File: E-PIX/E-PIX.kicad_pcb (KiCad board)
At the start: 6 copper layers, 40 x 40 mm, 47 parts, among them J1 USB_C_Receptacle_USB2.0, J2 BNO055, J3 ADC, J4 ADC, Q1 BSS138, Q2 BSS138, SW1 SW, SW2 SW_Push, U1 Conn_03x04, U2 Conn_03x04, U3 TC7WH241FK, U4 TC7WH241FK, U5 NJM7805SDL1, U6 AZ1117-3.3, U7 ESP32-C3-WROOM-02, U8 BTS6142D

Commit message: finish eeschema. start placing tips
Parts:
- removed G***: LOGO, Logo:Robo
- removed G***: LOGO, Logo:L6
- removed J3, J4: ADC, Connector_PinHeader_2.54mm:PinHeader_1x03_P2.54mm_Vertical
- added C10: 10u/50V/2012, Capacitor_SMD:C_0805_2012Metric, F.Cu at (123.2, 107.6)
- added C11: 22u/25V/2012, Capacitor_SMD:C_0805_2012Metric, F.Cu at (123.2, 89.8)
- added C12: 0.1u/25V, Capacitor_SMD:C_0603_1608Metric, B.Cu at (157.9, 101.3)
- added C9: 0.1u/25V, Capacitor_SMD:C_0603_1608Metric, B.Cu at (152.6, 89.8)
- added D4: CUHS20S60/2A/60V, Diode:Diode_US2H, F.Cu at (124.8, 115.9)
- added D5: CUHS20S60/2A/60V, Diode:Diode_US2H, F.Cu at (123.5, 94.9)
- added D6: CUHS20S60/2A/60V, Diode:Diode_US2H, F.Cu at (123.5, 98.7)
- added D7: LED, LED_SMD:LED_0603_1608Metric, B.Cu at (142.9, 91.0)
- added D8: WS2812B, LED_SMD:LED_WS2812B_PLCC4_5.0x5.0mm_P3.2mm, B.Cu at (145.4, 84.0)
- added Q3: AO3401A, Package_TO_SOT_SMD:SOT-23, F.Cu at (130.8, 93.7)
- added Q4: BSS138, Package_TO_SOT_SMD:SOT-23, F.Cu at (147.8, 129.8)
- added Q5: BSS138, Package_TO_SOT_SMD:SOT-23, F.Cu at (152.9, 129.8)
- added R14: 4.7, Resistor_SMD:R_0603_1608Metric, F.Cu at (128.4, 97.5)
- added R15: 2.2k, Resistor_SMD:R_0603_1608Metric, F.Cu at (149.2, 134.9)
- added R16: 2.2k, Resistor_SMD:R_0603_1608Metric, F.Cu at (141.7, 127.3)
- added R17: 2.2k, Resistor_SMD:R_0603_1608Metric, F.Cu at (137.3, 130.5)
- added R18: 2.2k, Resistor_SMD:R_0603_1608Metric, F.Cu at (141.7, 129.8)
- added R19: 10k, Resistor_SMD:R_0603_1608Metric, B.Cu at (157.6, 102.5)
- added R20: 100, Resistor_SMD:R_0603_1608Metric, B.Cu at (141.5, 94.9)
- added U10: Conn_03x04, Conn:PinHeader_03x04_P2.54mm_Vertical, F.Cu at (153.3, 122.9)
- C1: value 1u/50V/2012 -> 10u/35V; footprint Capacitor_SMD:C_0805_2012Metric -> Capacitor_SMD:C_1206_3216Metric
- C2: value 10u/50V/2012 -> C_Polarized; footprint Capacitor_SMD:C_0805_2012Metric -> Capacitor_THT:CP_Radial_D8.0mm_P3.50mm
- C3: value 10u/35V -> 47p; footprint Capacitor_SMD:C_0603_1608Metric -> Capacitor_SMD:C_0201_0603Metric
- C4: value 0.1u/25V -> 47p; footprint Capacitor_SMD:C_0603_1608Metric -> Capacitor_SMD:C_0201_0603Metric
- C5: value 22u/25V/2012 -> 0.1u/25V; footprint Capacitor_SMD:C_0805_2012Metric -> Capacitor_SMD:C_0603_1608Metric
- C6: value 1u/16V -> 1u/50V/2012; footprint Capacitor_SMD:C_0603_1608Metric -> Capacitor_SMD:C_0805_2012Metric
- C8, R9: moved to B.Cu
- D2: value CUHS20S60/2A/60V -> LED; footprint Diode:Diode_US2H -> LED_SMD:LED_0603_1608Metric; moved to B.Cu
- D3: value GREEN -> LED; moved to B.Cu
- J1: footprint Connector_USB:USB_C_Receptacle_XKB_U262-16XN-4BVC11 -> Connector_USB:USB_C_Receptacle_XKB_U262-16XN-4BVC11_with_model
- J2: value BNO055 -> DM3AT-SF-PEJM5; footprint Connector_PinHeader_2.54mm:PinHeader_1x05_P2.54mm_Vertical -> Connector_Card:microSD_HC_Hirose_DM3AT-SF-PEJM5
- Q1, Q2: value BSS138 -> 2SC4213; footprint Package_TO_SOT_SMD:SOT-23 -> Package_TO_SOT_SMD:SOT-323_SC-70
- R1: value 10k -> 5.1k
- R10: value 10k -> 47k
- R11: value 510 -> 47k
- R12, R13: value 2.2k -> 470k
- R3: value 5.1k -> 27
- R4: value 10k -> 27
- R5: value 2.2k -> 10k
- R6: value 2.2k -> 100; moved to B.Cu
- R8: value 10k -> 100; moved to B.Cu
- SW1: value SW -> SW_Push; footprint Connector_PinHeader_2.54mm:PinHeader_1x02_P2.54mm_Vertical -> Button_Switch_SMD:SKRPACE010; moved to B.Cu
- SW2: footprint Button_Switch_SMD:SW_Push_1P1T_NO_Vertical_Wuerth_434133025816 -> Button_Switch_SMD:SKRPACE010; moved to B.Cu
- U1: value Conn_03x04 -> FT231XS; footprint Conn:PinHeader_03x04_P2.54mm_Vertical -> Package_SO:SSOP-20_3.9x8.7mm_P0.635mm
- U2: value Conn_03x04 -> ESP32-S3-WROOM-1; footprint Conn:PinHeader_03x04_P2.54mm_Vertical -> Espressif:ESP32-S3-WROOM-1
- U3: value TC7WH241FK -> BTS6142D; footprint Logic:US-8 -> Package_TO_SOT_SMD:TO-252-4
- U4: value TC7WH241FK -> NJM7805SDL1; footprint Logic:US-8 -> Package_TO_SOT_SMD:TO-252-2
- U5: value NJM7805SDL1 -> TC7WH241FK; footprint Package_TO_SOT_SMD:TO-252-2 -> Logic:US-8
- U6: value AZ1117-3.3 -> TC7WH241FK; footprint Package_TO_SOT_SMD:SOT-223-3_TabPin2 -> Logic:US-8
- U7: value ESP32-C3-WROOM-02 -> AZ1117-3.3; footprint Espressif:ESP32-C3-WROOM-02 -> Package_TO_SOT_SMD:SOT-223-3_TabPin2
- U8: value BTS6142D -> ~; footprint Package_TO_SOT_SMD:TO-252-4 -> IMU:BNO055; moved to B.Cu
- U9: value ~ -> Conn_03x02; footprint IMU:BNO055 -> Conn:PinHeader_03x02_P2.54mm_Vertical; moved to F.Cu
- moved SW2 68.7 mm to (162.1, 102.5), turned to 90 degrees
- moved R5 67.2 mm to (156.7, 117.8), turned to 0 degrees
- moved H1 64.6 mm to (162.4, 122.4)
- moved H4 64.6 mm to (128.4, 122.4)
- moved R7 58.4 mm to (157.6, 120.3)
- moved U3 57.2 mm to (153.6, 109.7), turned to 90 degrees
- moved C2 54.5 mm to (161.0, 114.0), turned to -90 degrees
- moved J2 54.4 mm to (134.2, 109.9), turned to -90 degrees
- moved U4 54.0 mm to (136.0, 121.3), turned to 180 degrees
- moved C8 53.8 mm to (152.6, 92.4)
- moved R4 53.2 mm to (170.3, 97.5), turned to 0 degrees
- moved R11 52.7 mm to (147.4, 105.1), turned to 0 degrees
- moved U9 50.3 mm to (145.7, 108.9), turned to 0 degrees
- moved Q2 49.0 mm to (146.0, 103.8), turned to 0 degrees
- moved H2 48.7 mm to (162.4, 108.9)
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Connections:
- C1 pad 2: VDD -> +3V3
- C2 pad 1: GND -> VDD
- C2 pad 2: +5V -> GND
- C3 pad 1: +3V3 -> GND
- C3 pad 2: GND -> Net-(U1-USBDM)
- C4 pad 1: +5V -> GND
- C4 pad 2: GND -> Net-(U1-USBDP)
- C5 pad 1: +3V3 -> GND
- C5 pad 2: GND -> +3V3
- C6 pad 1: Net-(U7-EN/CHIP_PU) -> GND
- C6 pad 2: GND -> VSS
- C7 pad 1: +3V3 -> +5V
- C8 pad 1: /RST -> /EN
- D1 pad 1: VDD -> +5V
- D1 pad 2: +5V -> Net-(D1-A)
- D2 pad 1: +5V -> Net-(D2-K)
- D2 pad 2: Net-(D2-A) -> VSS
- D3 pad 1: GND -> Net-(D3-K)
- D3 pad 2: Net-(D3-A) -> +3V3
- J1 pad A4: Net-(D2-A) -> Net-(D1-A)
- J1 pad A9: Net-(D2-A) -> Net-(D1-A)
- J1 pad B4: Net-(D2-A) -> Net-(D1-A)
- J1 pad B9: Net-(D2-A) -> Net-(D1-A)
- J1 pad S1: unconnected-(J1-SHIELD-PadS1) -> GND
- J2 pad 1: GND -> unconnected-(J2-DAT2-Pad1)
- J2 pad 2: +3V3 -> /CS
- J2 pad 3: /SCL -> /MOSI
- J2 pad 4: /SDA -> +3V3
- J2 pad 5: /BNO055RST -> /CLK
- Q1 pad 1: +3V3 -> Net-(Q1-B)
- Q1 pad 2: /ICS1_3V3 -> /RTS
- Q1 pad 3: /ICS1_5V -> /EN
- Q2 pad 1: +3V3 -> Net-(Q2-B)
- Q2 pad 2: /ICS2_3V3 -> /DTR
- Q2 pad 3: /ICS2_5V -> /BOOT
- R1 pad 1: GND -> Net-(J1-CC1)
- R1 pad 2: /ADC1 -> GND
- R10 pad 1: Net-(U8-IS) -> Net-(Q1-B)
- R10 pad 2: GND -> /DTR
- R11 pad 1: +3V3 -> Net-(Q2-B)
- R11 pad 2: Net-(D3-A) -> /RTS
- R12 pad 1: +5V -> GND
- R12 pad 2: /ICS1_5V -> /DTR
- R13 pad 1: +5V -> GND
- R13 pad 2: /ICS2_5V -> /RTS
- R2 pad 1: Net-(J1-CC1) -> Net-(J1-CC2)
- R3 pad 1: Net-(J1-CC2) -> /D-
- R3 pad 2: GND -> Net-(U1-USBDM)
- R4 pad 1: GND -> Net-(U1-USBDP)
- R4 pad 2: /ADC2 -> /D+
- R5 pad 1: +3V3 -> Net-(U3-IN)
- R5 pad 2: /ICS1_3V3 -> /EN_Power
- R6 pad 1: +3V3 -> Net-(D2-K)
- R6 pad 2: /ICS2_3V3 -> GND
- R7 pad 1: +3V3 -> Net-(U3-IS)
- R7 pad 2: Net-(U7-EN/CHIP_PU) -> GND
- R8 pad 1: +3V3 -> Net-(D3-K)
- R8 pad 2: Net-(U7-GPIO8) -> GND
- R9 pad 1: Net-(SW1A-B) -> /EN
- R9 pad 2: Net-(U8-IN) -> +3V3
- SW1 pad 1: GND -> /EN
- SW1 pad 2: Net-(SW1A-B) -> GND
- SW2 pad 1: /RST -> /SW
- U1 pad 1: GND -> /DTR
- U1 pad 2: VSS -> /RTS
- U1 pad 3: /ICS1_5V -> +3V3
- U2 pad 2: VSS -> +3V3
- U2 pad 3: /ICS2_5V -> /EN
- U3 pad 1: /EN1 -> VSS
- U3 pad 2: /ICS1_3V3 -> Net-(U3-IN)
- U3 pad 3: /ICS1_3V3 -> VDD
- U3 pad 4: GND -> Net-(U3-IS)
- U3 pad 5: /TX1 -> VSS
- U4 pad 1: /EN2 -> VSS
- U4 pad 2: /ICS2_3V3 -> GND
- U4 pad 3: /ICS2_3V3 -> +5V
- U5 pad 1: VDD -> /EN1
- U5 pad 2: GND -> /ICS1_3V3
- U5 pad 3: +5V -> /ICS1_3V3
- U6 pad 1: GND -> /EN2
- U6 pad 2: +3V3 -> /ICS2_3V3
- U6 pad 3: +5V -> /ICS2_3V3
- U7 pad 1: +3V3 -> GND
- U7 pad 2: Net-(U7-EN/CHIP_PU) -> +3V3
- U7 pad 3: /ADC1 -> VSS
- U8 pad 1: VSS -> +3V3
- U8 pad 2: Net-(U8-IN) -> GND
- U8 pad 3: VDD -> /SDA
- U8 pad 4: Net-(U8-IS) -> /SCL
- U8 pad 5: VSS -> /BNO_RST
- U9 pad 1: +3V3 -> GND
- U9 pad 2: GND -> VSS
- U9 pad 3: /SDA -> /ICS1_5V
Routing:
- net +3V3: track 93.1 -> 0.00 mm
- net /BNO055RST: track 57.5 -> 0.00 mm, vias 2 -> 0
- net +5V: track 48.6 -> 0.00 mm, vias 3 -> 0
- net /EN2: track 39.6 -> 0.00 mm, vias 2 -> 0
- net /RST: track 33.9 -> 0.00 mm, vias 2 -> 0
- net /RX2: track 33.8 -> 0.00 mm, vias 2 -> 0
- net /RX1: track 31.4 -> 0.00 mm, vias 2 -> 0
- net /TX1: track 31.3 -> 0.00 mm, vias 2 -> 0
- net /EN1: track 29.6 -> 0.00 mm, vias 2 -> 0
- net /TX2: track 28.2 -> 0.00 mm, vias 2 -> 0
- net /SDA: track 25.9 -> 0.00 mm, vias 1 -> 0
- net VDD: track 25.7 -> 0.00 mm, vias 2 -> 0
- net /SCL: track 25.0 -> 0.00 mm, vias 1 -> 0
- net Net-(D2-A): track 21.5 -> 0.00 mm, vias 3 -> 0
- net /ICS1_5V: track 21.2 -> 0.00 mm, vias 2 -> 0
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- removed copper zone on B.Cu, net GND
- removed copper zone on F.Cu, net GND
- removed copper zone on In1.Cu, net GND
- removed copper zone on In2.Cu, net GND
- removed copper zone on In3.Cu, net GND
- removed copper zone on In4.Cu, net GND
- removed copper zone on F.Cu, net VDD
- removed copper zone on B.Cu, net VSS
- removed copper zone on F.Cu, net VSS
- removed copper zone on In1.Cu, net VSS
- removed copper zone on In2.Cu, net VSS
- removed copper zone on In3.Cu, net VSS
- removed copper zone on In4.Cu, net VSS
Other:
- board size 40 x 40 mm -> 40.1 x 45 mm
- copper layers 6 -> 2
- board text removed: "+"
- board text removed: "-"
- board text removed: "2024.04.06"
- board text removed: "ADC1/3V3/GND"
- board text removed: "ADC2/3V3/GND"
- board text removed: "AE-BNO055-BO"
- board text removed: "BRST/SDA/SCL/3V3/GND"
- board text removed: "CPU"
- board text removed: "ControlBoard3"
- board text removed: "GND/VDD/ICS2"
- board text removed: "HumanRobot"
- board text removed: "ICS1/VDD/GND"
- board text removed: "RESET"
- board text removed: "SW"
- board text removed: "VIN"

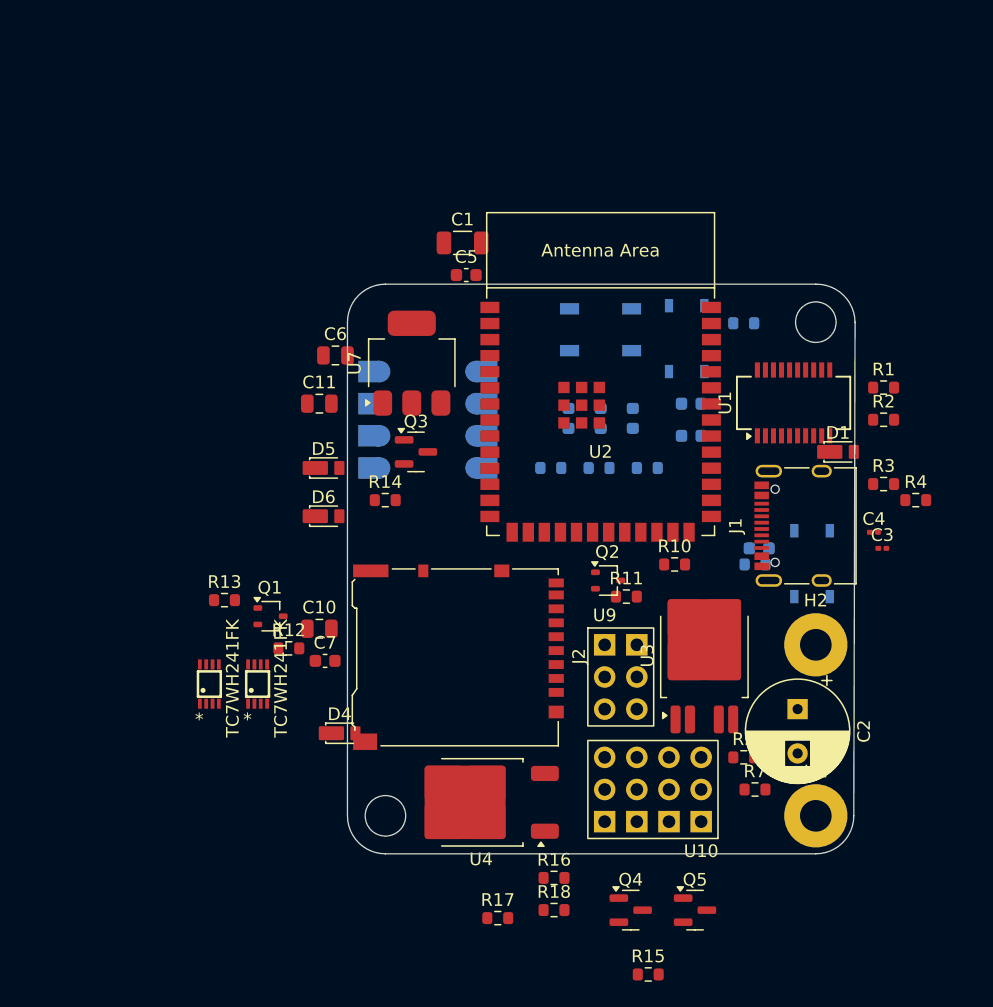
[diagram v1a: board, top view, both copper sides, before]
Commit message: place 3v3 reg and USB-TTY serial
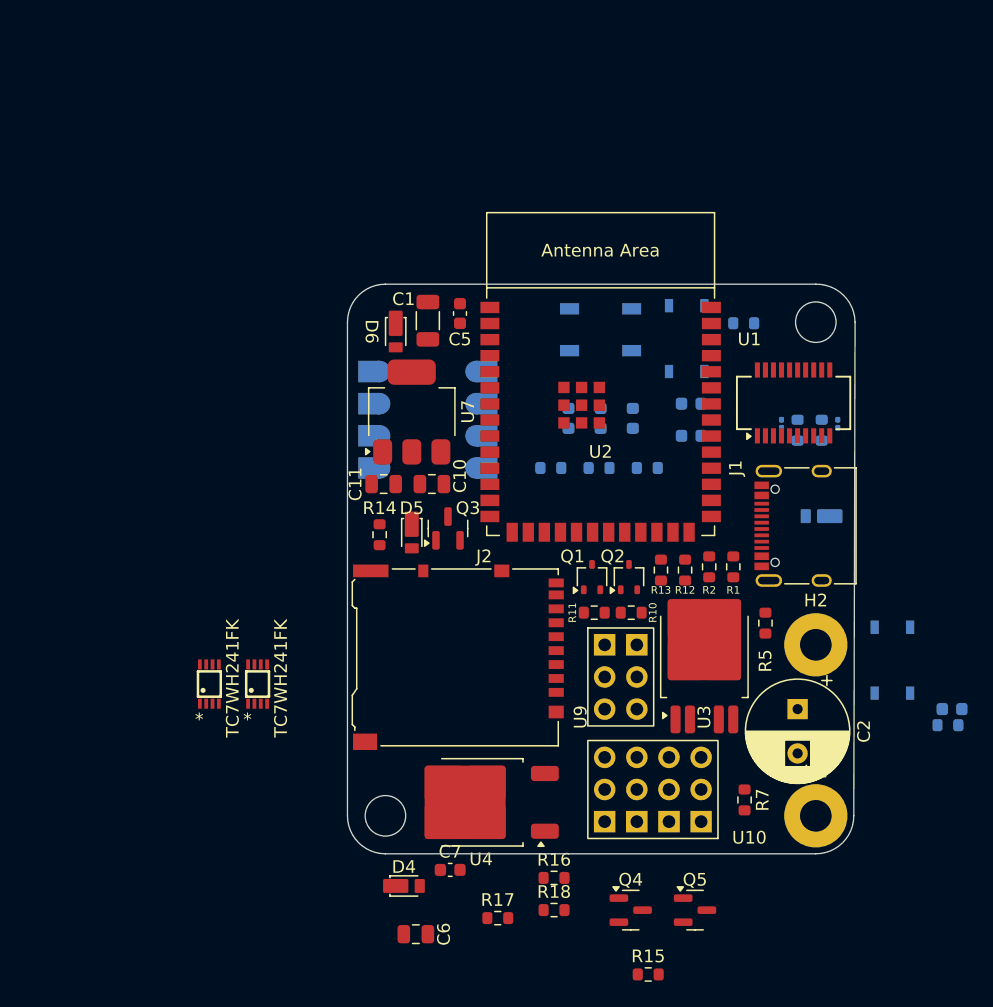
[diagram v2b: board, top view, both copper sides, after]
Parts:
- C3, C4, D1, R3, R4: moved to B.Cu
- moved C6 46.2 mm to (130.8, 131.8)
- moved R13 34.6 mm to (150.2, 103.0), turned to 90 degrees
- moved R12 31.9 mm to (152.1, 103.0), turned to 90 degrees
- moved Q1 25.6 mm to (144.7, 103.5), turned to 90 degrees
- moved R19 19.8 mm to (172.8, 115.2)
- moved C12 19.8 mm to (173.2, 114.0)
- moved C7 19.2 mm to (133.5, 126.7)
- moved R1 18.5 mm to (155.9, 102.7), turned to -90 degrees
- moved R2 18.0 mm to (154.0, 102.7), turned to -90 degrees
- moved D6 15.7 mm to (129.2, 84.1), turned to -90 degrees
- moved C10 14.5 mm to (132.1, 96.2)
- moved D4 13.1 mm to (129.9, 127.9)
- moved C3 12.7 mm to (159.7, 91.4), turned to 90 degrees
- moved R5 10.7 mm to (158.4, 107.2), turned to 90 degrees
- moved SW2 9.92 mm to (168.4, 110.1)
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
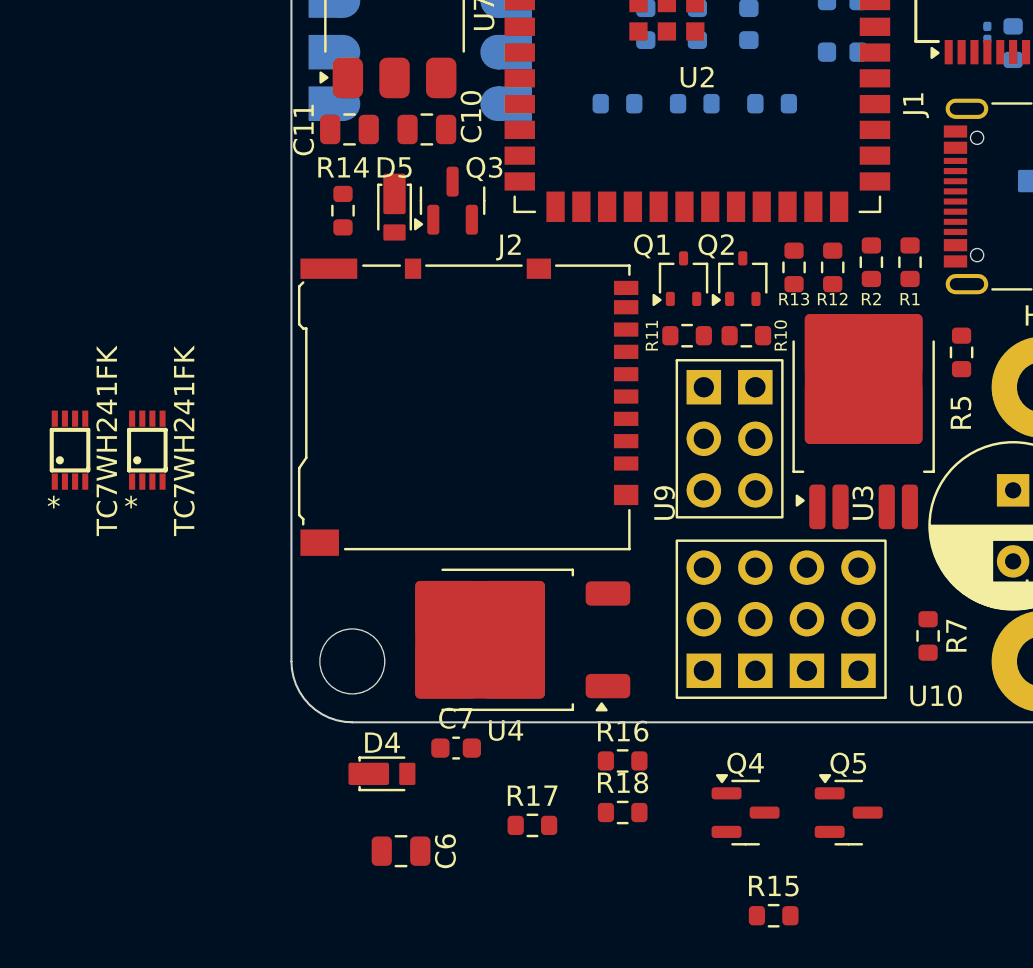
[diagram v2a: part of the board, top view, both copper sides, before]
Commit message: update some pin mappings of ESP
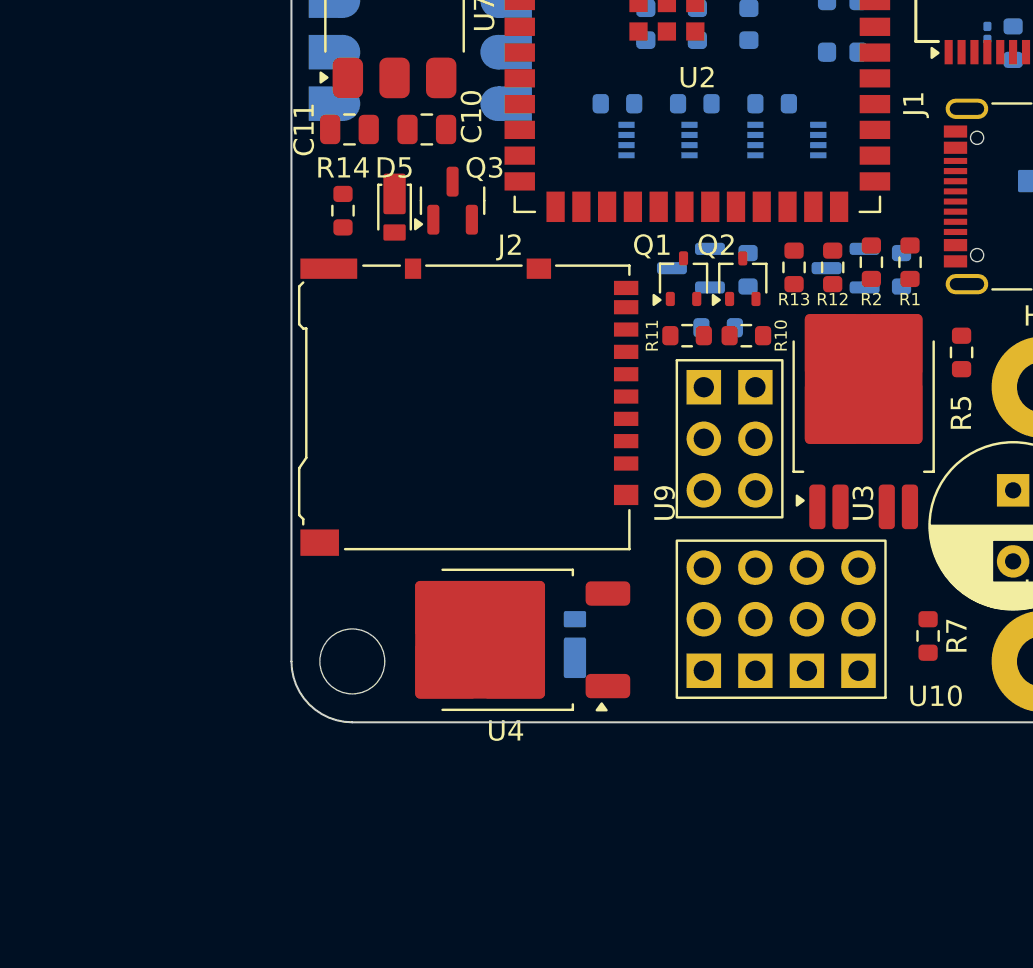
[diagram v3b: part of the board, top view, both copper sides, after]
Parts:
- C6, C7, D4, Q4, Q5, R15, R16, R17, R18, U5, U6: moved to B.Cu
- moved U6 35.0 mm to (149.8, 96.7), turned to -90 degrees
- moved R17 32.9 mm to (155.5, 103.1), turned to -90 degrees
- moved U5 32.8 mm to (143.5, 96.7), turned to -90 degrees
- moved R15 31.8 mm to (147.9, 103.1), turned to -90 degrees
- moved Q4 27.0 mm to (145.1, 103.0), turned to 180 degrees
- moved R18 26.9 mm to (154.0, 105.9), turned to 180 degrees
- moved Q5 26.8 mm to (152.7, 103.0), turned to 180 degrees
- moved R16 21.9 mm to (146.4, 106.0), turned to 180 degrees
- moved D4 11.4 mm to (139.4, 121.6), turned to 90 degrees
- moved C6 10.2 mm to (135.9, 122.9)
- moved C7 6.84 mm to (136.1, 120.3), turned to 180 degrees
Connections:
- U2 pad 22: unconnected-(U2-IO14-Pad22) -> /EN1
- U2 pad 23: unconnected-(U2-IO21-Pad23) -> /EN2
- U2 pad 26: unconnected-(U2-IO45-Pad26) -> /EN_Power
- U2 pad 28: unconnected-(U2-IO35-Pad28) -> /SW
- U2 pad 39: /SW -> unconnected-(U2-IO1-Pad39)
- U2 pad 4: /EN1 -> unconnected-(U2-IO4-Pad4)
- U2 pad 5: /EN2 -> unconnected-(U2-IO5-Pad5)
- U2 pad 6: /EN_Power -> unconnected-(U2-IO6-Pad6)

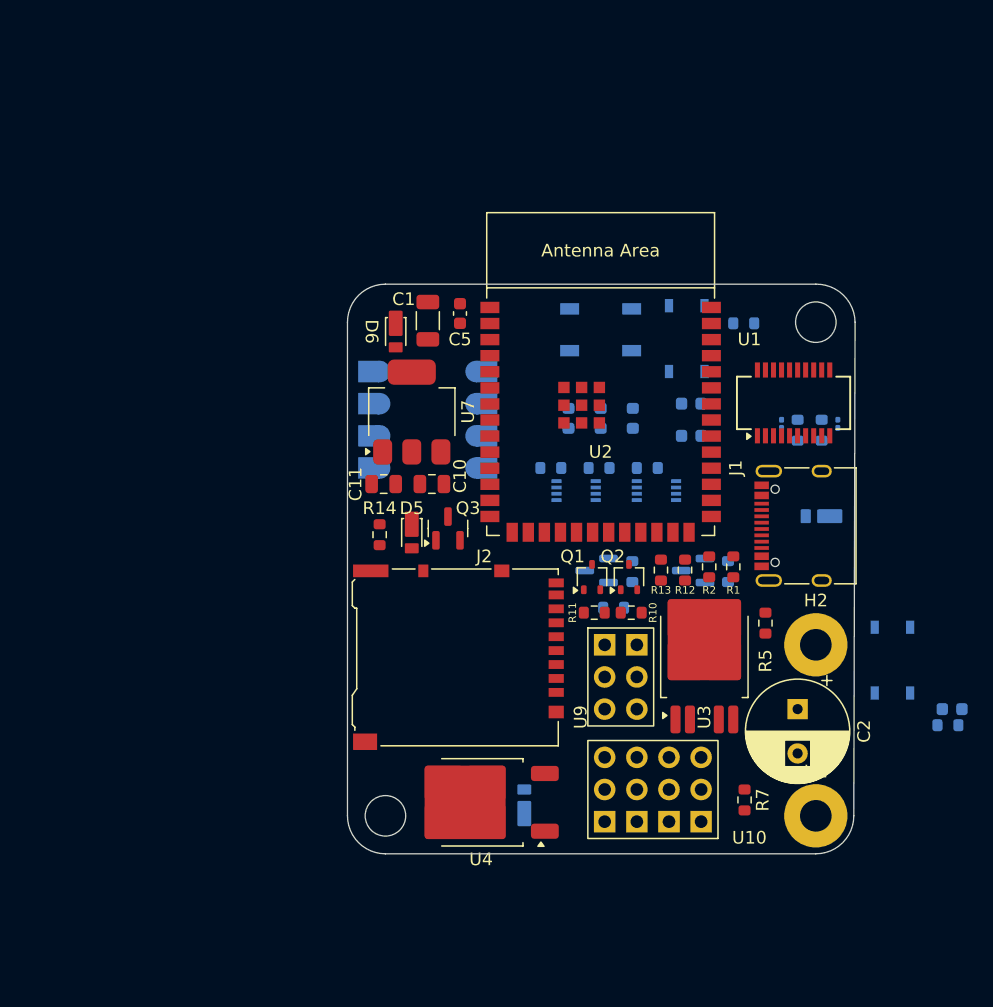
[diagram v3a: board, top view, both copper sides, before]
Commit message: place all the tips
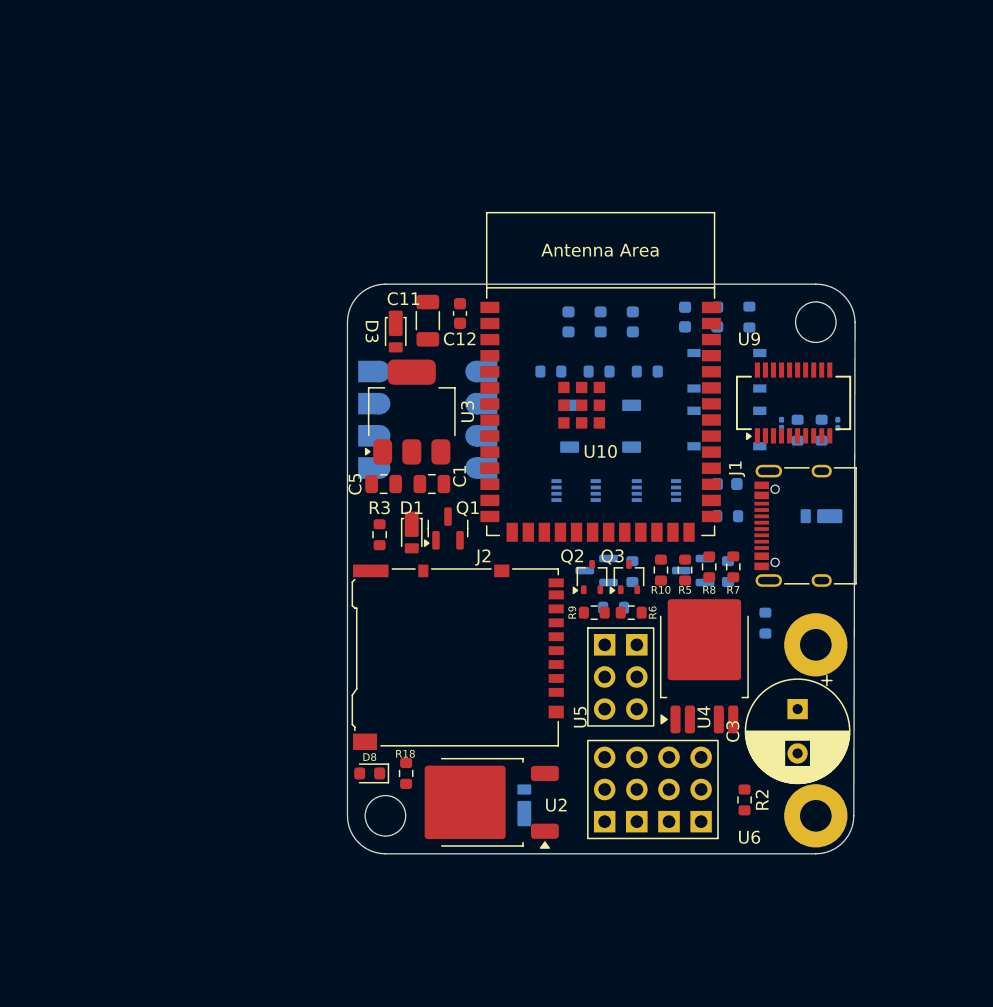
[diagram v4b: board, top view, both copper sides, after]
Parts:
- added D8: LED, LED_SMD:LED_0603_1608Metric, F.Cu at (127.2, 119.0)
- added R18: 10k, Resistor_SMD:R_0603_1608Metric, F.Cu at (130.0, 119.0)
- R1: renamed from R5; moved to B.Cu
- U7: renamed from U5; value TC7WH241FK -> U7
- U8: renamed from U6; value TC7WH241FK -> U8
- moved C6 25.1 mm to (155.4, 96.2)
- moved R11 24.0 mm to (155.4, 98.7), turned to 0 degrees
- moved SW1 22.5 mm to (155.4, 91.8), turned to 180 degrees
- moved C9 9.40 mm to (152.1, 83.0), turned to 90 degrees
- moved D4 7.62 mm to (147.9, 83.4)
- moved D6 7.62 mm to (145.4, 91.6)
- moved D7 7.62 mm to (142.9, 83.4)
- moved D9 7.62 mm to (145.4, 83.4)
- moved R14 7.62 mm to (141.5, 87.3)
- moved R19 7.62 mm to (145.3, 87.3)
- moved R4 7.62 mm to (149.1, 87.3)
- moved C10 7.14 mm to (154.6, 83.0), turned to 90 degrees
- moved SW2 4.07 mm to (155.4, 87.2), turned to 180 degrees
- moved R15 0.67 mm to (157.2, 83.0), turned to 90 degrees
- renumbered C10 to C1, C9 to C10, C1 to C11, C5 to C12, C6 to C2, C2 to C3, C7 to C4, C11 to C5, C12 to C6, C3 to C7, C4 to C8, C8 to C9, D5 to D1, D4 to D2, D6 to D3, D2 to D4, D1 to D5, D8 to D6, D3 to D9, Q3 to Q1, Q1 to Q2, Q2 to Q3, R13 to R10, R19 to R11, R3 to R12, R4 to R13, R20 to R14, R9 to R15, R15 to R16, R16 to R17, R8 to R19, R7 to R2, R17 to R20, R18 to R21, R14 to R3, R6 to R4, R12 to R5, R10 to R6, R1 to R7, R2 to R8, R11 to R9, SW2 to SW1, SW1 to SW2, U8 to U1, U2 to U10, U4 to U2, U7 to U3, U3 to U4, U9 to U5, U10 to U6, U1 to U9
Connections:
- J2 pad 10: (no net) -> GND
- J2 pad 11: (no net) -> GND
- J2 pad 9: (no net) -> /SWA
